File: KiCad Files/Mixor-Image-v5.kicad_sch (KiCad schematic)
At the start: 51 parts, among them J1 Conn_01x03_Male, J2 Conn_01x03_Female, J3 Conn_01x03_Male, J4 Conn_01x03_Female, U1 TL072, U2 TL072

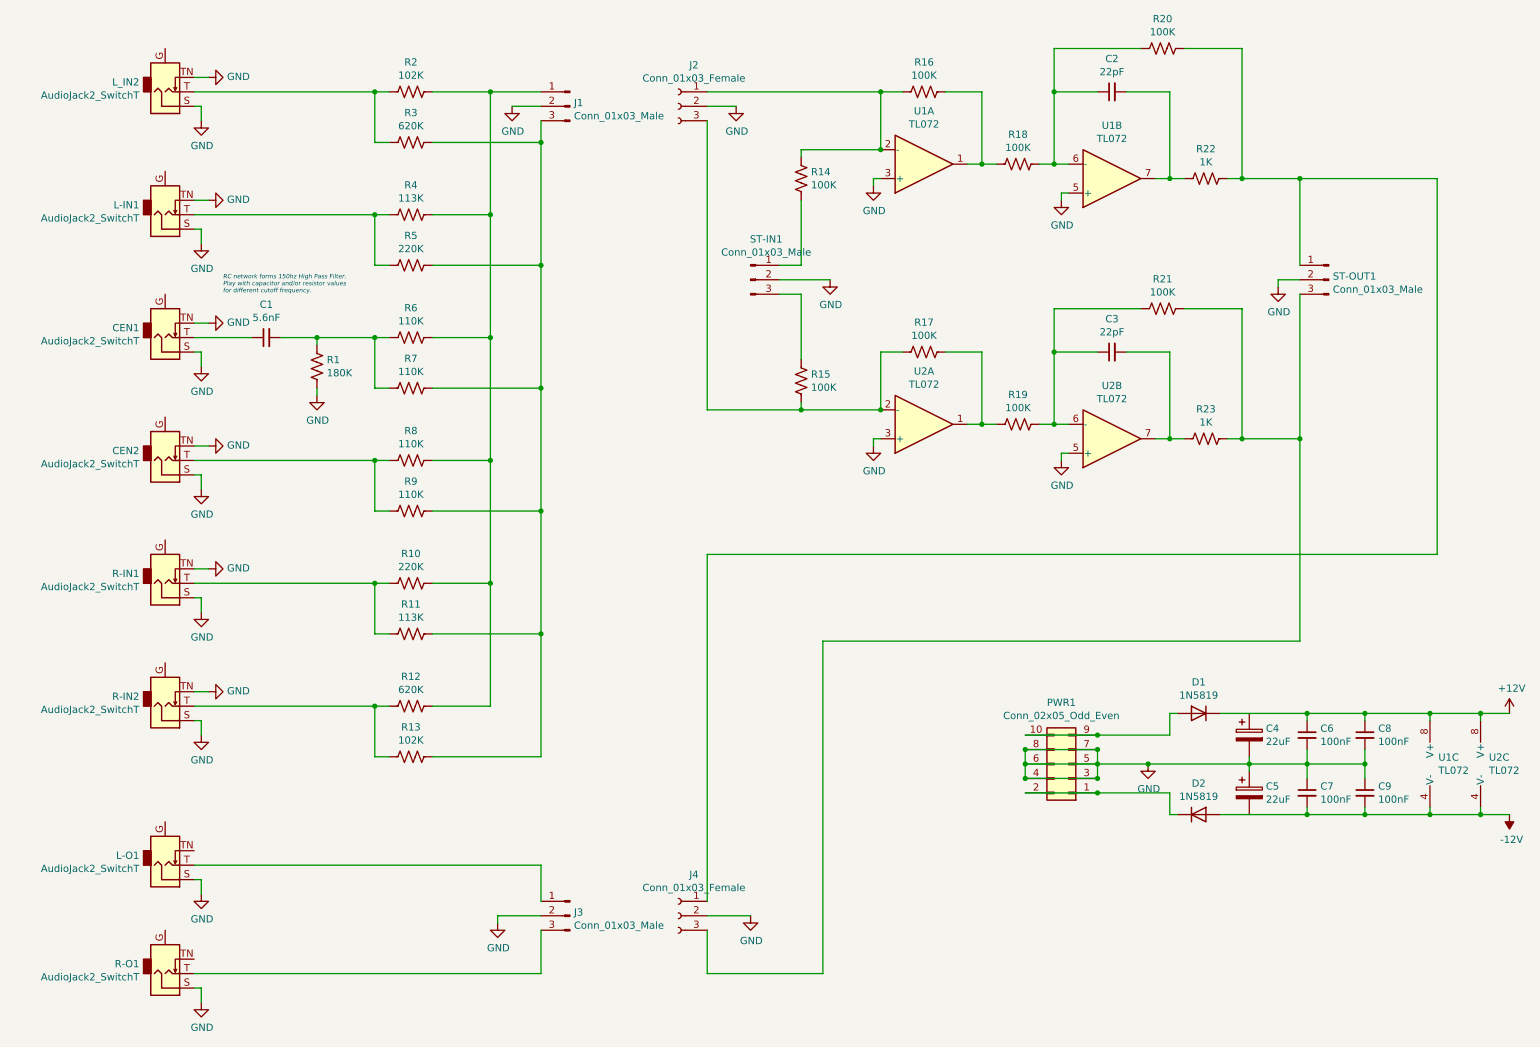
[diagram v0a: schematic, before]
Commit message: only 1 error committing before flipping components so all SMD are on the same side
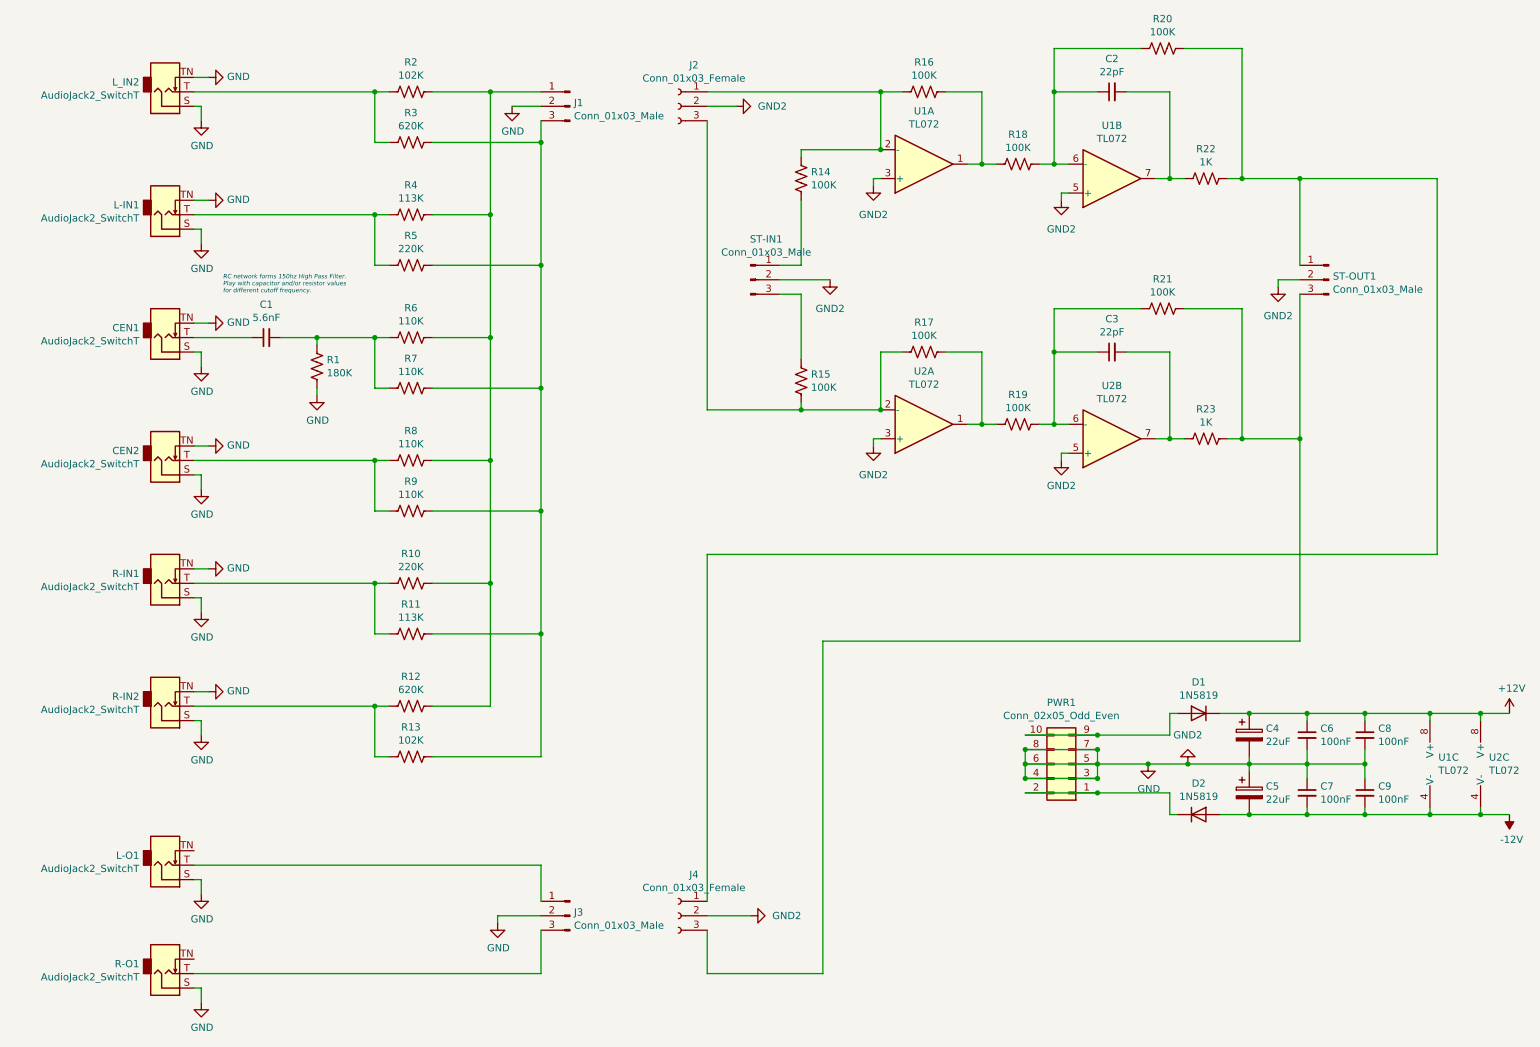
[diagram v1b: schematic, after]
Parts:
- CEN1, CEN2, L-IN1, L-O1, L_IN2, R-IN1, R-IN2, R-O1: symbol Connector_Audio:AudioJack2_Ground_SwitchT -> Connector_Audio:AudioJack2_SwitchT
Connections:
- net +12V: now also C4.1
- net -12V: now also C5.2
